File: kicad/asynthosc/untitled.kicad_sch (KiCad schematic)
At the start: 6 parts, among them J13 AudioJack3, U8 H11L1

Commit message: sch: add spi nor, display connection, and more footprints
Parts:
- J13: footprint (none) -> asynthosc:Jack_3.5mm_4legs_XKB_PJ-3410_Vertical
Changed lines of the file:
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@@
 		(pin "2"
 		)
-		(instances)
 	)
 	(symbol
@@
 		(pin "1"
 		)
-		(instances)
 	)
 	(symbol
@@
 			)
 		)
-		(property "Footprint" ""
+		(property "Footprint" "asynthosc:Jack_3.5mm_4legs_XKB_PJ-3410_Vertical"
 			(at 185.42 50.8 0)
 			(effects
@@
 		(pin "T"
 		)
-		(instances)
 	)
 	(symbol
@@
 		(pin "2"
 		)
-		(instances)
 	)
 	(symbol
@@
 		(pin "1"
 		)
-		(instances)
-	)
-	(symbol
+	)
+	(symbol

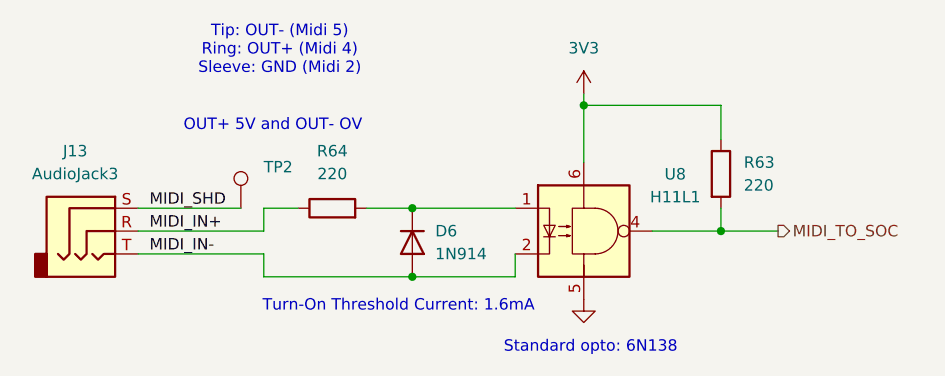
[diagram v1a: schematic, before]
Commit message: sch: update footprint links
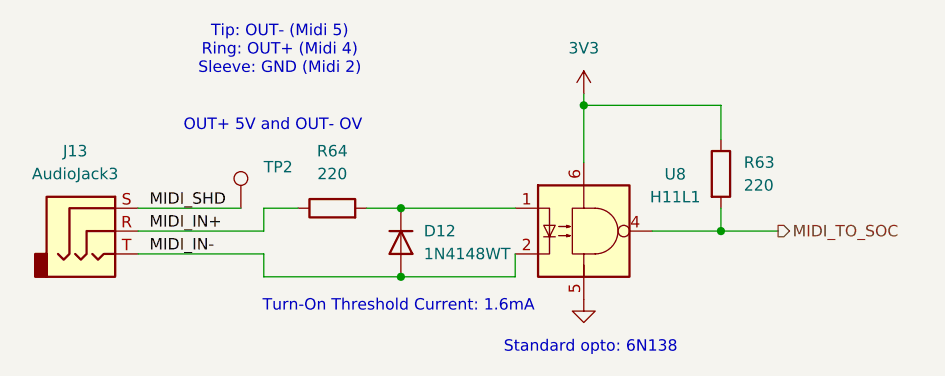
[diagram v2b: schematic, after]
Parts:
- removed D6: 1N914, Diode_THT:D_DO-35_SOD27_P7.62mm_Horizontal, symbol Diode:1N914
- added D12: 1N4148WT, Diode_SMD:D_SOD-523, symbol Diode:1N4148WT
- J13: footprint asynthosc:Jack_3.5mm_4legs_XKB_PJ-3410_Vertical -> asynthosc:Jack_3.5mm_3legs_XKB_PJ-3411_Vertical
- R63, R64: footprint (none) -> Resistor_SMD:R_0402_1005Metric
- TP2: footprint (none) -> TestPoint:TestPoint_Pad_D1.0mm
- U8: footprint (none) -> Package_DIP:SMDIP-6_W9.53mm
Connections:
- net MIDI_IN-: now also D12.2 (A)
- net at R64.2, U8.1: now also D12.1 (K)
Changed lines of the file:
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@@
 	(paper "A4")
 	(junction
-		(at 220.98 55.88)
+		(at 219.71 48.26)
 		(diameter 0)
 		(color 0 0 0 0)
@@
 	)
 	(junction
+		(at 219.71 55.88)
+		(diameter 0)
+		(color 0 0 0 0)
+	)
+	(junction
 		(at 255.27 50.8)
 		(diameter 0)
 		(color 0 0 0 0)
 	)
-	(junction
-		(at 220.98 48.26)
-		(diameter 0)
-		(color 0 0 0 0)
-	)
 	(wire
 		(pts
@@
 	(wire
 		(pts
-			(xy 204.47 55.88) (xy 220.98 55.88)
+			(xy 204.47 55.88) (xy 219.71 55.88)
 		)
 		(stroke
@@
 	(wire
 		(pts
-			(xy 215.9 48.26) (xy 220.98 48.26)
+			(xy 219.71 55.88) (xy 232.41 55.88)
+		)
+		(stroke
+			(width 0)
+			(type default)
+		)
+	)
+	(wire
+		(pts
+			(xy 215.9 48.26) (xy 219.71 48.26)
 		)
 		(stroke
@@
 	(wire
 		(pts
+			(xy 219.71 48.26) (xy 232.41 48.26)
+		)
+		(stroke
+			(width 0)
+			(type default)
+		)
+	)
+	(wire
+		(pts
 			(xy 190.5 50.8) (xy 204.47 50.8)
 		)
@@
 	(wire
 		(pts
-			(xy 232.41 55.88) (xy 220.98 55.88)
-		)
-		(stroke
-			(width 0)
-			(type default)
-		)
-	)
-	(wire
-		(pts
 			(xy 204.47 48.26) (xy 208.28 48.26)
-		)
-		(stroke
-			(width 0)
-			(type default)
-		)
-	)
-	(wire
-		(pts
-			(xy 220.98 48.26) (xy 232.41 48.26)
 		)
 		(stroke
@@
 			)
 		)
-		(property "Footprint" ""
+		(property "Footprint" "Package_DIP:SMDIP-6_W9.53mm"
 			(at 237.744 50.8 0)
 			(effects
@@
 	)
 	(symbol
-		(lib_id "Diode:1N914")
-		(at 220.98 52.07 270)
+		(lib_id "Diode:1N4148WT")
+		(at 219.71 52.07 270)
 		(unit 1)
 		(exclude_from_sim no)
@@
 		(dnp no)
 		(fields_autoplaced yes)
-		(property "Reference" "D6"
-			(at 223.52 50.7999 90)
+		(property "Reference" "D12"
+			(at 222.25 50.7999 90)
 			(effects
 				(font
@@
 			)
 		)
-		(property "Value" "1N914"
-			(at 223.52 53.3399 90)
+		(property "Value" "1N4148WT"
+			(at 222.25 53.3399 90)
 			(effects
 				(font
@@
 			)
 		)
-		(property "Footprint" "Diode_THT:D_DO-35_SOD27_P7.62mm_Horizontal"
-			(at 216.535 52.07 0)
-			(effects
-				(font
-					(size 1.27 1.27)
-				)
-				(hide yes)
-			)
-		)
-		(property "Datasheet" "http://www.vishay.com/docs/85622/1n914.pdf"
-			(at 220.98 52.07 0)
-			(effects
-				(font
-					(size 1.27 1.27)
-				)
-				(hide yes)
-			)
-		)
-		(property "Description" "100V 0.3A Small Signal Fast Switching Diode, DO-35"
-			(at 220.98 52.07 0)
+		(property "Footprint" "Diode_SMD:D_SOD-523"
+			(at 215.265 52.07 0)
+			(effects
+				(font
+					(size 1.27 1.27)
+				)
+				(hide yes)
+			)
+		)
+		(property "Datasheet" "https://www.diodes.com/assets/Datasheets/ds30396.pdf"
+			(at 219.71 52.07 0)
+			(effects
+				(font
+					(size 1.27 1.27)
+				)
+				(hide yes)
+			)
+		)
+		(property "Description" "75V 0.15A Fast switching Diode, SOD-523"
+			(at 219.71 52.07 0)
 			(effects
 				(font
@@
 		)
 		(property "Sim.Device" "D"
-			(at 220.98 52.07 0)
+			(at 219.71 52.07 0)
 			(effects
 				(font
@@
 		)
 		(property "Sim.Pins" "1=K 2=A"
-			(at 220.98 52.07 0)
+			(at 219.71 52.07 0)
 			(effects
 				(font
@@
 		)
 		(pin "1"
+		)
+		(instances
+			(project ""
+				(path "/d73e377a-a016-415f-8824-91cc6e4907b9/e5b5a411-a62d-4190-89e5-07a84042033c"
+					(reference "D12")
+					(unit 1)
+				)
+			)
 		)
 	)
@@
 			)
 		)
-		(property "Footprint" "asynthosc:Jack_3.5mm_4legs_XKB_PJ-3410_Vertical"
+		(property "Footprint" "asynthosc:Jack_3.5mm_3legs_XKB_PJ-3411_Vertical"
 			(at 185.42 50.8 0)
 			(effects
@@
 			)
 		)
-		(property "Footprint" ""
+		(property "Footprint" "Resistor_SMD:R_0402_1005Metric"
 			(at 212.09 50.038 90)
 			(effects
@@
 			)
 		)
-		(property "Footprint" ""
+		(property "Footprint" "TestPoint:TestPoint_Pad_D1.0mm"
 			(at 207.01 48.26 0)
 			(effects
@@
 			)
 		)
-		(property "Footprint" ""
+		(property "Footprint" "Resistor_SMD:R_0402_1005Metric"
 			(at 253.492 44.45 90)
 			(effects

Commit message: sch: change stm32 for smaller one, create smaller jumper footprint
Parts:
- D12: Manufacturer (none) -> Diodes Inc; RefNum (none) -> 1N4148WT
- J13: Manufacturer (none) -> XKB; RefNum (none) -> PJ-3411
- U8: Manufacturer (none) -> OnSemi
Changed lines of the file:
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@@
+			)
+		)
+		(property "LCSC" ""
+			(at 240.03 50.8 0)
+			(effects
+				(font
+					(size 1.27 1.27)
+				)
+				(hide yes)
+			)
+		)
+		(property "Manufacturer" "OnSemi"
+			(at 240.03 50.8 0)
+			(effects
+				(font
+					(size 1.27 1.27)
+				)
+				(hide yes)
 			)
 		)
@@
 			)
 		)
+		(property "LCSC" ""
+			(at 219.71 52.07 0)
+			(effects
+				(font
+					(size 1.27 1.27)
+				)
+				(hide yes)
+			)
+		)
+		(property "Manufacturer" "Diodes Inc"
+			(at 219.71 52.07 0)
+			(effects
+				(font
+					(size 1.27 1.27)
+				)
+				(hide yes)
+			)
+		)
+		(property "RefNum" "1N4148WT"
+			(at 219.71 52.07 0)
+			(effects
+				(font
+					(size 1.27 1.27)
+				)
+				(hide yes)
+			)
+		)
 		(pin "2"
 		)
@@
 			)
 		)
+		(property "LCSC" ""
+			(at 185.42 50.8 0)
+			(effects
+				(font
+					(size 1.27 1.27)
+				)
+				(hide yes)
+			)
+		)
+		(property "Manufacturer" "XKB"
+			(at 185.42 50.8 0)
+			(effects
+				(font
+					(size 1.27 1.27)
+				)
+				(hide yes)
+			)
+		)
+		(property "RefNum" "PJ-3411 "
+			(at 185.42 50.8 0)
+			(effects
+				(font
+					(size 1.27 1.27)
+				)
+				(hide yes)
+			)
+		)
 		(pin "S"
 		)
@@
 			)
 		)
+		(property "LCSC" ""
+			(at 212.09 48.26 0)
+			(effects
+				(font
+					(size 1.27 1.27)
+				)
+				(hide yes)
+			)
+		)
+		(property "Manufacturer" ""
+			(at 212.09 48.26 0)
+			(effects
+				(font
+					(size 1.27 1.27)
+				)
+				(hide yes)
+			)
+		)
 		(pin "1"
 		)
@@
 			)
 		)
+		(property "LCSC" ""
+			(at 201.93 48.26 0)
+			(effects
+				(font
+					(size 1.27 1.27)
+				)
+				(hide yes)
+			)
+		)
+		(property "Manufacturer" ""
+			(at 201.93 48.26 0)
+			(effects
+				(font
+					(size 1.27 1.27)
+				)
+				(hide yes)
+			)
+		)
 		(pin "1"
 		)
@@
 			(at 255.27 44.45 0)
 			(effects
+				(font
+					(size 1.27 1.27)
+				)
+				(hide yes)
+			)
+		)
+		(property "LCSC" ""
+			(at 255.27 44.45 0)
+			(effects
+				(font
+					(size 1.27 1.27)
+				)
+				(hide yes)
+			)
+		)
+		(property "Manufacturer" ""
+			(at 255.27 44.45 0)
+			(effects

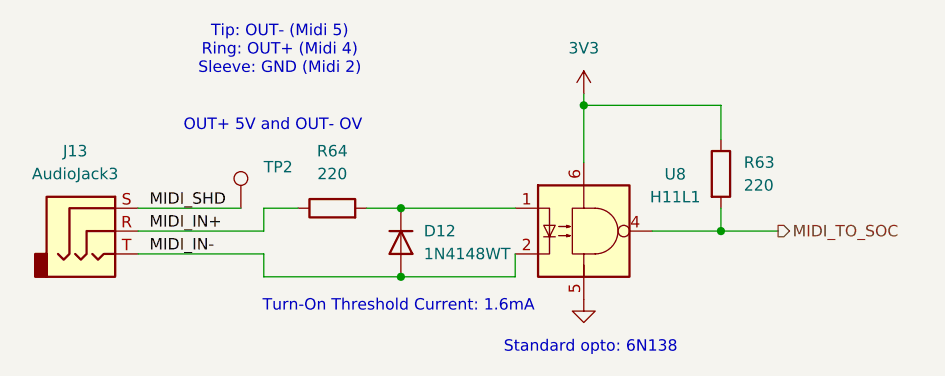
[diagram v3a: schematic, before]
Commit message: bom: update bom for lcsc
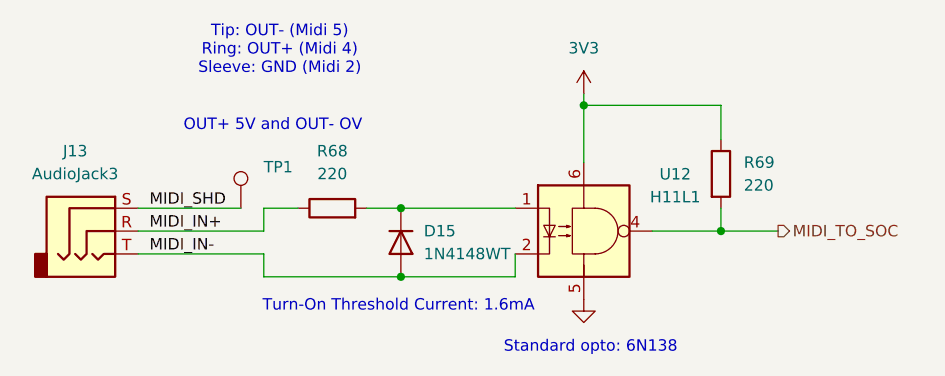
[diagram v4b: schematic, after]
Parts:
- D15: renamed from D12; Manufacturer Diodes Inc -> LGE
- R68: renamed from R64; RefNum (none) -> _generic_
- R69: renamed from R63; RefNum (none) -> _generic_
- TP1: renamed from TP2; RefNum (none) -> _na_
- renumbered U8 to U12
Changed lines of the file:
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@@
 		(dnp no)
 		(fields_autoplaced yes)
-		(property "Reference" "U8"
+		(property "Reference" "U12"
 			(at 250.19 44.4814 0)
 			(effects
@@
 		)
 		(pin "2"
+		)
+		(instances
+			(project ""
+				(path "/d73e377a-a016-415f-8824-91cc6e4907b9/e5b5a411-a62d-4190-89e5-07a84042033c"
+					(reference "U12")
+					(unit 1)
+				)
+			)
 		)
 	)
@@
 		(dnp no)
 		(fields_autoplaced yes)
-		(property "Reference" "D12"
+		(property "Reference" "D15"
 			(at 222.25 50.7999 90)
 			(effects
@@
 			)
 		)
-		(property "Manufacturer" "Diodes Inc"
+		(property "Manufacturer" "LGE"
 			(at 219.71 52.07 0)
 			(effects
@@
 			(project ""
 				(path "/d73e377a-a016-415f-8824-91cc6e4907b9/e5b5a411-a62d-4190-89e5-07a84042033c"
-					(reference "D12")
+					(reference "D15")
 					(unit 1)
 				)
@@
 		(pin "T"
 		)
+		(instances
+			(project ""
+				(path "/d73e377a-a016-415f-8824-91cc6e4907b9/e5b5a411-a62d-4190-89e5-07a84042033c"
+					(reference "J13")
+					(unit 1)
+				)
+			)
+		)
 	)
 	(symbol
@@
 		(dnp no)
 		(fields_autoplaced yes)
-		(property "Reference" "R64"
+		(property "Reference" "R68"
 			(at 212.09 41.91 90)
 			(effects
@@
 			)
 		)
+		(property "RefNum" "_generic_"
+			(at 212.09 48.26 0)
+			(effects
+				(font
+					(size 1.27 1.27)
+				)
+				(hide yes)
+			)
+		)
 		(pin "1"
 		)
 		(pin "2"
+		)
+		(instances
+			(project ""
+				(path "/d73e377a-a016-415f-8824-91cc6e4907b9/e5b5a411-a62d-4190-89e5-07a84042033c"
+					(reference "R68")
+					(unit 1)
+				)
+			)
 		)
 	)
@@
 		(dnp no)
 		(fields_autoplaced yes)
-		(property "Reference" "TP2"
+		(property "Reference" "TP1"
 			(at 204.47 43.6879 0)
 			(effects
@@
 			)
 		)
+		(property "RefNum" "_na_"
+			(at 201.93 48.26 0)
+			(effects
+				(font
+					(size 1.27 1.27)
+				)
+				(hide yes)
+			)
+		)
 		(pin "1"
+		)
+		(instances
+			(project ""
+				(path "/d73e377a-a016-415f-8824-91cc6e4907b9/e5b5a411-a62d-4190-89e5-07a84042033c"
+					(reference "TP1")
+					(unit 1)
+				)
+			)
 		)
 	)
@@
 		(dnp no)
 		(fields_autoplaced yes)
-		(property "Reference" "#PWR091"
+		(property "Reference" "#PWR0116"
 			(at 240.03 39.37 0)
 			(effects
@@
 			(project "asynthosc"
 				(path "/d73e377a-a016-415f-8824-91cc6e4907b9/e5b5a411-a62d-4190-89e5-07a84042033c"
-					(reference "#PWR091")
+					(reference "#PWR0116")
 					(unit 1)
 				)
@@
 		(dnp no)
 		(fields_autoplaced yes)
-		(property "Reference" "R63"
+		(property "Reference" "R69"
 			(at 257.81 43.1799 0)
 			(effects
@@
 		)
 		(property "Manufacturer" ""
+			(at 255.27 44.45 0)
+			(effects
+				(font
+					(size 1.27 1.27)
+				)
+				(hide yes)
+			)
+		)
+		(property "RefNum" "_generic_"
 			(at 255.27 44.45 0)
 			(effects
@@
 			(project "asynthosc"
 				(path "/d73e377a-a016-415f-8824-91cc6e4907b9/e5b5a411-a62d-4190-89e5-07a84042033c"
-					(reference "R63")
+					(reference "R69")
 					(unit 1)
 				)
@@
 		(dnp no)
 		(fields_autoplaced yes)
-		(property "Reference" "#PWR090"
+		(property "Reference" "#PWR0117"
 			(at 240.03 64.77 0)
 			(effects
@@
 			(project "asynthosc"
 				(path "/d73e377a-a016-415f-8824-91cc6e4907b9/e5b5a411-a62d-4190-89e5-07a84042033c"
-					(reference "#PWR090")
+					(reference "#PWR0117")
 					(unit 1)
 				)

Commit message: pcb: place and change some components for easier routing
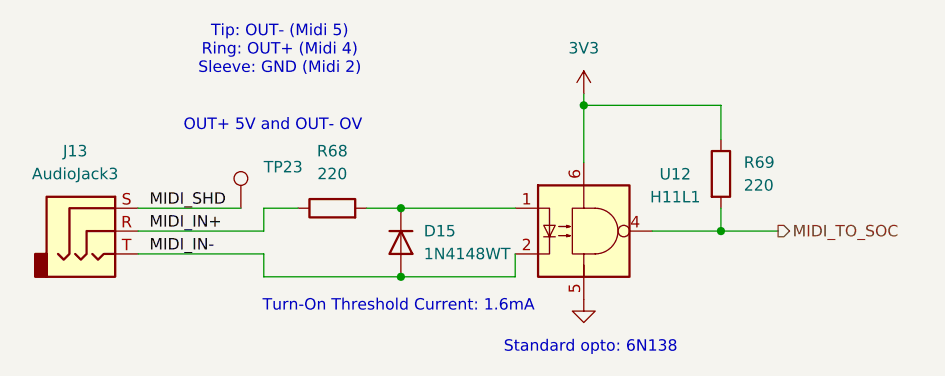
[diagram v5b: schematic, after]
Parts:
- renumbered TP1 to TP23
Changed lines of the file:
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@@
 		(dnp no)
 		(fields_autoplaced yes)
-		(property "Reference" "TP1"
+		(property "Reference" "TP23"
 			(at 204.47 43.6879 0)
 			(effects
@@
 			(project ""
 				(path "/d73e377a-a016-415f-8824-91cc6e4907b9/e5b5a411-a62d-4190-89e5-07a84042033c"
-					(reference "TP1")
+					(reference "TP23")
 					(unit 1)
 				)
@@
 		(dnp no)
 		(fields_autoplaced yes)
-		(property "Reference" "#PWR0116"
+		(property "Reference" "#PWR0119"
 			(at 240.03 39.37 0)
 			(effects
@@
 			(project "asynthosc"
 				(path "/d73e377a-a016-415f-8824-91cc6e4907b9/e5b5a411-a62d-4190-89e5-07a84042033c"
-					(reference "#PWR0116")
+					(reference "#PWR0119")
 					(unit 1)
 				)
@@
 		(dnp no)
 		(fields_autoplaced yes)
-		(property "Reference" "#PWR0117"
+		(property "Reference" "#PWR0120"
 			(at 240.03 64.77 0)
 			(effects
@@
 			(project "asynthosc"
 				(path "/d73e377a-a016-415f-8824-91cc6e4907b9/e5b5a411-a62d-4190-89e5-07a84042033c"
-					(reference "#PWR0117")
+					(reference "#PWR0120")
 					(unit 1)
 				)

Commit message: bom: update mfr, serials and lcsc fields
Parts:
- D15: LCSC (none) -> C970342
- J13: LCSC (none) -> C381132
- U12: LCSC (none) -> C899473
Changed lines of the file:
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@@
 			)
 		)
-		(property "LCSC" ""
+		(property "LCSC" "C899473"
 			(at 240.03 50.8 0)
 			(effects
@@
 			)
 		)
-		(property "LCSC" ""
+		(property "LCSC" "C970342"
 			(at 219.71 52.07 0)
 			(effects
@@
 			)
 		)
-		(property "LCSC" ""
-			(at 185.42 50.8 0)
-			(effects
+		(property "LCSC" "C381132"
+			(at 185.42 50.8 0)
+			(effects

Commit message: bom: sch: pcb: update for sourcing in jlc pcba services
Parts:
- U12: LCSC C899473 -> C22376095; Manufacturer OnSemi -> JSMSEMI; RefNum H11L1SM -> H11L1S-JSM
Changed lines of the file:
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@@
 			)
 		)
-		(property "RefNum" "H11L1SM"
+		(property "RefNum" "H11L1S-JSM"
 			(at 240.03 50.8 0)
 			(effects
@@
 			)
 		)
-		(property "LCSC" "C899473"
+		(property "LCSC" "C22376095"
 			(at 240.03 50.8 0)
 			(effects
@@
 			)
 		)
-		(property "Manufacturer" "OnSemi"
+		(property "Manufacturer" "JSMSEMI"
 			(at 240.03 50.8 0)
 			(effects
